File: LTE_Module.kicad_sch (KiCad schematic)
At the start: 57 parts, among them J4 Conn_Coaxial, J8 SIM_Card, Q3 MMBT3904, Q4 BC849, Q5 MMBT3904, Q6 MMBT3904, U10 MIC29302AWD, U6 A7670E, U9 AMS1117-3.3

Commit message: finelized scematics
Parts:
- removed C12, C15, C16: 22uF, Capacitor_SMD:C_0603_1608Metric, symbol Device:C
- removed C13: 100pF, Capacitor_SMD:C_0805_2012Metric, symbol Device:C
- removed J8: SIM_Card, Connector_JAE:JAE_SIM_Card_SF72S006, symbol Connector:SIM_Card
- removed R14, R15, R16: 22R, Resistor_SMD:R_0603_1608Metric, symbol Device:R
- added C41, C43, C45: 22uF, Capacitor_SMD:C_0603_1608Metric, symbol Device:C
- added C44: 100pF, Capacitor_SMD:C_0805_2012Metric, symbol Device:C
- added J2: JAE_SIM_Card_SF72S006, Connector_JAE:JAE_SIM_Card_SF72S006, symbol Connector:JAE_SIM_Card_SF72S006
- added R24, R25, R26: 22R, Resistor_SMD:R_0603_1608Metric, symbol Device:R
- TP11, TP12, TP17, TP2, TP7, TP8, TP9: footprint TestPoint:TestPoint_Pad_D2.5mm -> TestPoint:TestPoint_Pad_D2.0mm
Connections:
- net PWR is gone; now on net 3V3: R41.1
- net CLK_EN: now also J2.C3 (CLK), R25.2
- net DATA_EN: now also J2.C7 (I/O), R24.1
- net GND: now also C41.2, C43.2, C44.2, C45.2, J2.C5 (GND)
- net RST_EN: now also J2.C2 (RST), R26.1
- net SIM_CLK: now also C41.1, R25.1
- net SIM_DATA: now also C43.1, R24.2
- net SIM_RST: now also C45.1, R26.2
- net SIM_VCC: now also C44.1, J2.C1 (VCC)
- no-connect marks 23 -> 27
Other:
- moved on the sheet: C25, C26, C31, C32, C33, C34, R51, R52, TP17, U10, U9

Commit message: mostly layouted
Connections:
- net 3V3: now also TP17.1
- net GND: no longer TP17.1
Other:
- moved on the sheet: TP17
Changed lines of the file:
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@@
+	(wire
+		(pts
+			(xy 233.68 82.55) (xy 233.68 85.09)
+		)
+		(stroke
+			(width 0)
+			(type default)
+		)
+	)
 	(wire
 		(pts
@@
 	(symbol
 		(lib_id "Connector:TestPoint")
-		(at 233.68 92.71 180)
+		(at 233.68 82.55 0)
 		(unit 1)
 		(exclude_from_sim no)
@@
 		(fields_autoplaced yes)
 		(property "Reference" "TP17"
-			(at 236.22 94.7419 0)
-			(effects
-				(font
-					(size 1.27 1.27)
-				)
-				(justify right)
+			(at 236.22 77.9779 0)
+			(effects
+				(font
+					(size 1.27 1.27)
+				)
+				(justify left)
 			)
 		)
 		(property "Value" "TestPoint"
-			(at 236.22 97.2819 0)
-			(effects
-				(font
-					(size 1.27 1.27)
-				)
-				(justify right)
+			(at 236.22 80.5179 0)
+			(effects
+				(font
+					(size 1.27 1.27)
+				)
+				(justify left)
 			)
 		)
 		(property "Footprint" "TestPoint:TestPoint_Pad_D2.0mm"
-			(at 228.6 92.71 0)
+			(at 238.76 82.55 0)
 			(effects
 				(font
@@
 		)
 		(property "Datasheet" "~"
-			(at 228.6 92.71 0)
+			(at 238.76 82.55 0)
 			(effects
 				(font
@@
 		)
 		(property "Description" "test point"
-			(at 233.68 92.71 0)
+			(at 233.68 82.55 0)
 			(effects
 				(font
@@
 		)
 		(property "Availability" ""
-			(at 233.68 92.71 0)
+			(at 233.68 82.55 0)
 			(effects
 				(font
@@
 		)
 		(property "Check_prices" ""
-			(at 233.68 92.71 0)
+			(at 233.68 82.55 0)
 			(effects
 				(font
@@
 		)
 		(property "Description_1" ""
-			(at 233.68 92.71 0)
+			(at 233.68 82.55 0)
 			(effects
 				(font
@@
 		)
 		(property "MANUFACTURER" ""
-			(at 233.68 92.71 0)
+			(at 233.68 82.55 0)
 			(effects
 				(font
@@
 		)
 		(property "MAXIMUM_PACKAGE_HEIGHT" ""
-			(at 233.68 92.71 0)
+			(at 233.68 82.55 0)
 			(effects
 				(font
@@
 		)
 		(property "MF" ""
-			(at 233.68 92.71 0)
+			(at 233.68 82.55 0)
 			(effects
 				(font
@@
 		)
 		(property "MP" ""
-			(at 233.68 92.71 0)
+			(at 233.68 82.55 0)
 			(effects
 				(font
@@
 		)
 		(property "PARTREV" ""
-			(at 233.68 92.71 0)
+			(at 233.68 82.55 0)
 			(effects
 				(font
@@
 		)
 		(property "Package" ""
-			(at 233.68 92.71 0)
+			(at 233.68 82.55 0)
 			(effects
 				(font
@@
 		)
 		(property "Price" ""
-			(at 233.68 92.71 0)
+			(at 233.68 82.55 0)
 			(effects
 				(font
@@
 		)
 		(property "SNAPEDA_PN" ""
-			(at 233.68 92.71 0)
+			(at 233.68 82.55 0)
 			(effects
 				(font
@@
 		)
 		(property "STANDARD" ""
-			(at 233.68 92.71 0)
+			(at 233.68 82.55 0)
 			(effects
 				(font
@@
 		)
 		(property "SnapEDA_Link" ""
-			(at 233.68 92.71 0)
-			(effects
-				(font
+			(at 233.68 82.55 0)
+			(effects
+				(font

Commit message: pre remobing sd card
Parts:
- removed TP12, TP2: TestPoint, TestPoint:TestPoint_Pad_D2.0mm, symbol Connector:TestPoint
- TP11, TP17, TP7, TP8, TP9: footprint TestPoint:TestPoint_Pad_D2.0mm -> TestPoint:TestPoint_Pad_D1.5mm
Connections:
- net CLK_EN: no longer names the net of J2.C3 (CLK), R25.2
- net RST_EN: no longer names the net of J2.C2 (RST), R26.1

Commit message: mostly finished layout
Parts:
- removed TP17: TestPoint, TestPoint:TestPoint_Pad_D1.5mm, symbol Connector:TestPoint
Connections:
- net +5V: no longer TP11.1, U6.24 (VBUS)
- net DATA_EN: no longer names the net of J2.C7 (I/O), R24.1
- new net: TP11.1, U6.24 (VBUS)
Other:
- moved on the sheet: TP11

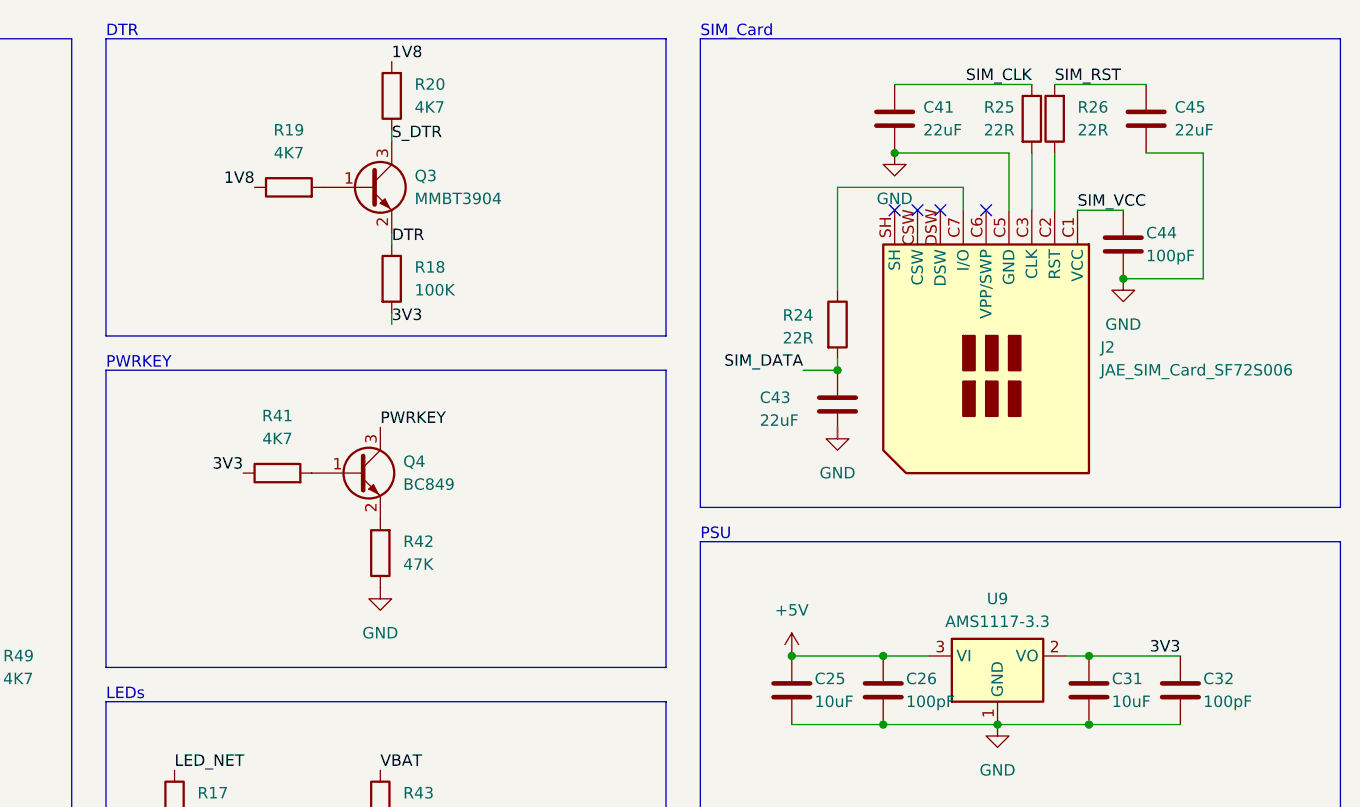
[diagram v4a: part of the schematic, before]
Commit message: updated schematics:
Fixed bug with PWKEY of LTE module

Fixed big with power
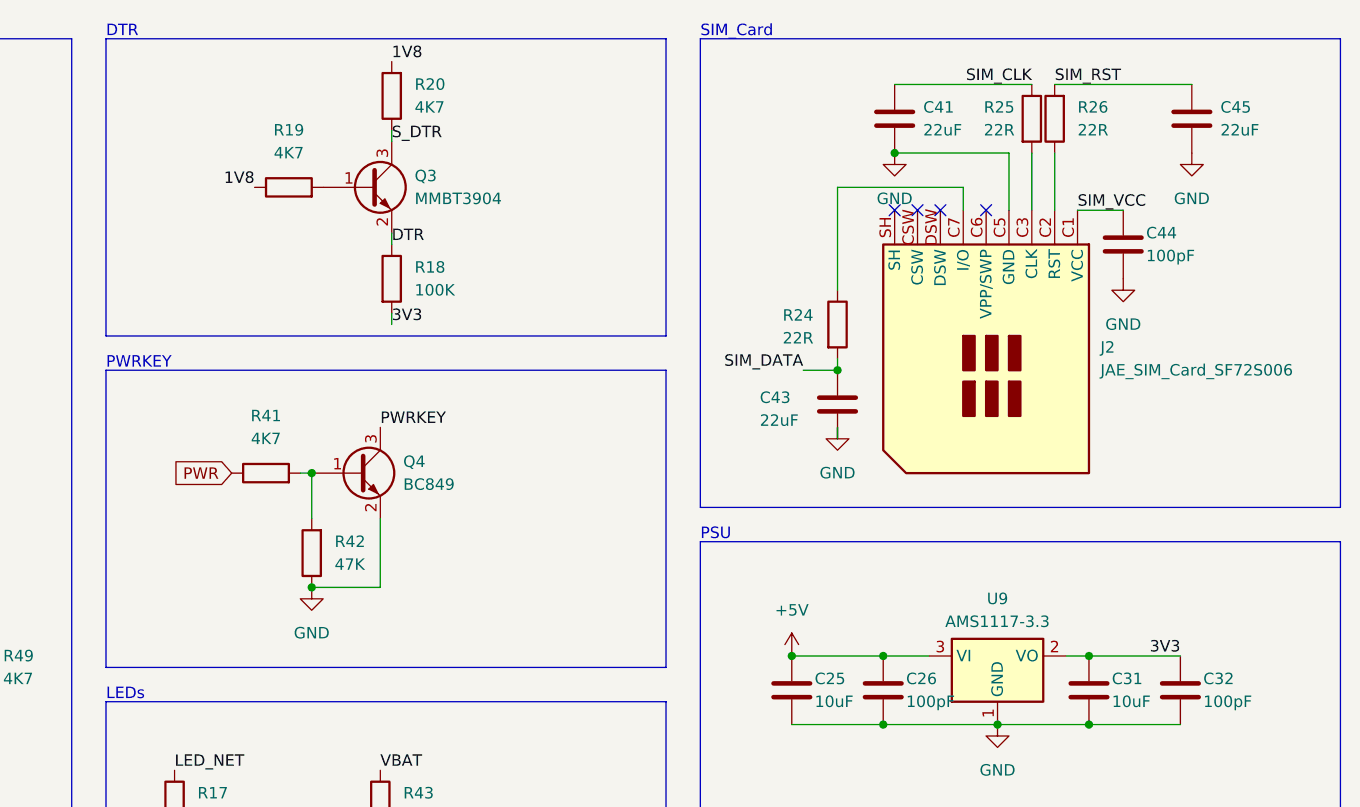
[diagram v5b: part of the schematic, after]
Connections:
- net 3V3: no longer R41.1
- net GND: now also Q4.2 (E)
- net at Q4.1 (B), R41.2: now also R42.2
- new net PWR: R41.1
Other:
- moved on the sheet: C45, R41, R42

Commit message: first new layout
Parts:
- removed C25, C31: 10uF, Capacitor_SMD:C_1206_3216Metric, symbol Device:C
- removed C26, C32: 100pF, Capacitor_SMD:C_0805_2012Metric, symbol Device:C
- removed C41, C43, C45: 22uF, Capacitor_SMD:C_0603_1608Metric, symbol Device:C
- removed U9: AMS1117-3.3, Package_TO_SOT_SMD:SOT-223-3_TabPin2, symbol Regulator_Linear:AMS1117-3.3
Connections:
- net 3V3 renamed +3V3
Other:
- moved on the sheet: C33, C34, R24, R51, R52, U10
